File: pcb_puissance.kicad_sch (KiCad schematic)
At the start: 29 parts, among them J1 1735882, J2 1735882, J3 1735882, J4 1735882, J5 1735882, J6 1735882, J7 1735882, J8 1735882, K1 SRD-05VDC-SL-C

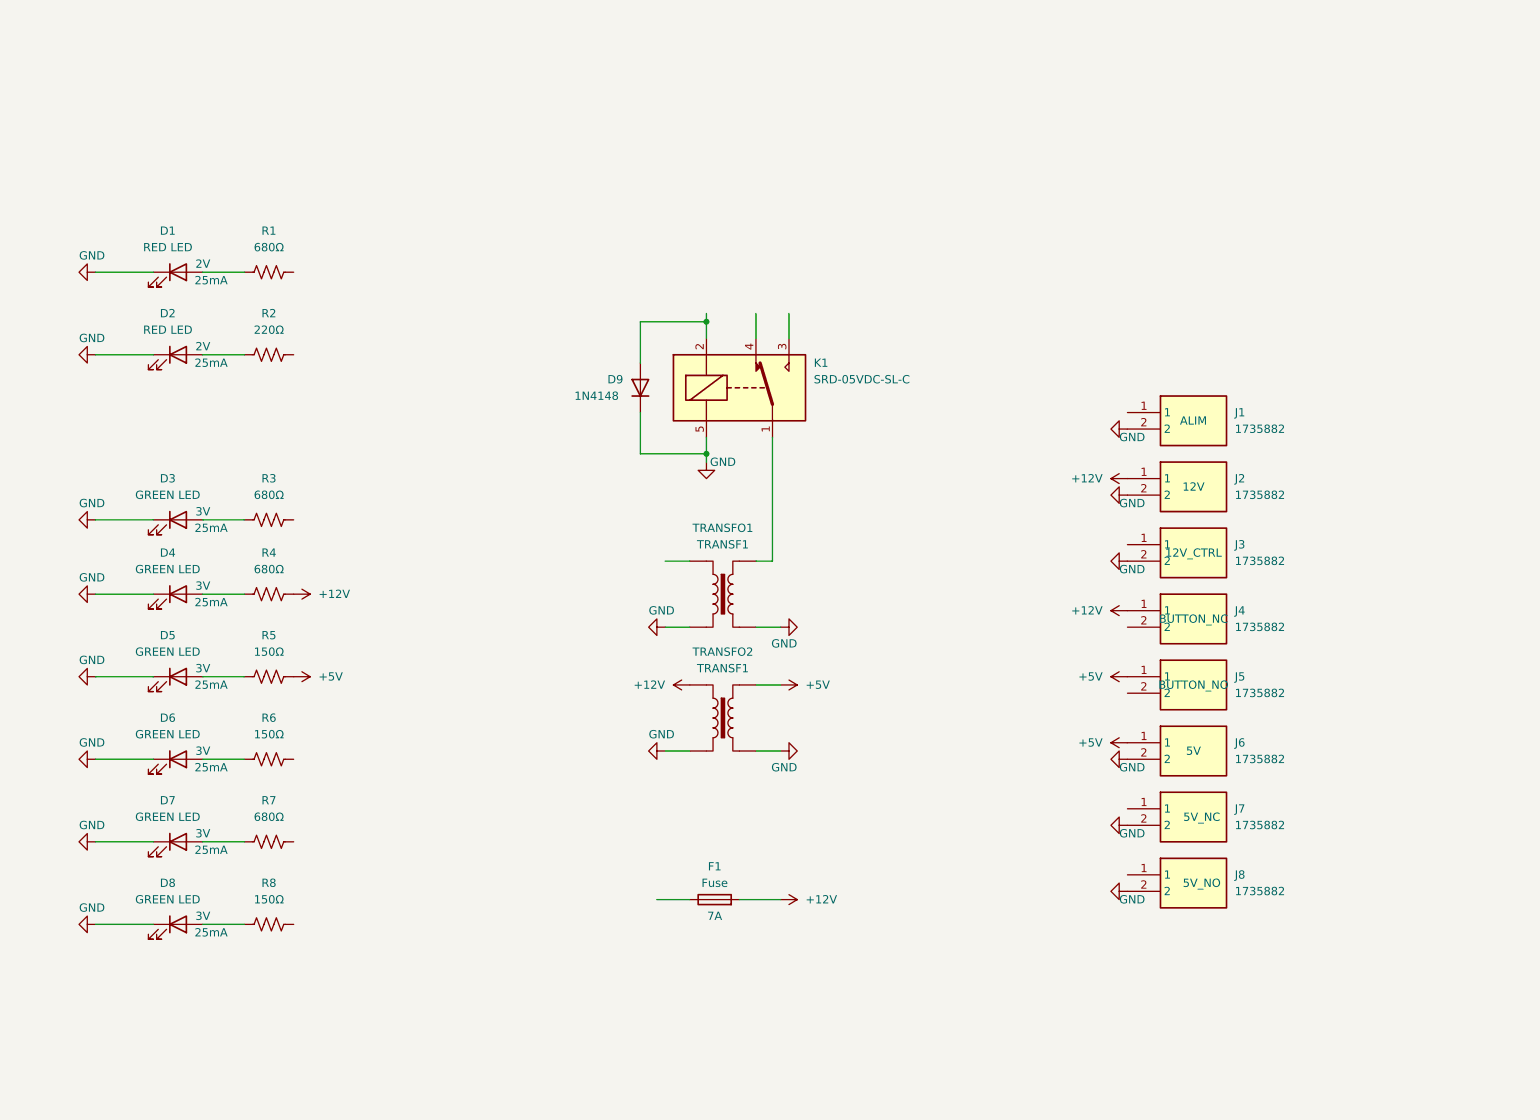
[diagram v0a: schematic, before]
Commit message: changements connecteur CI + placement empreintes et routage PCB
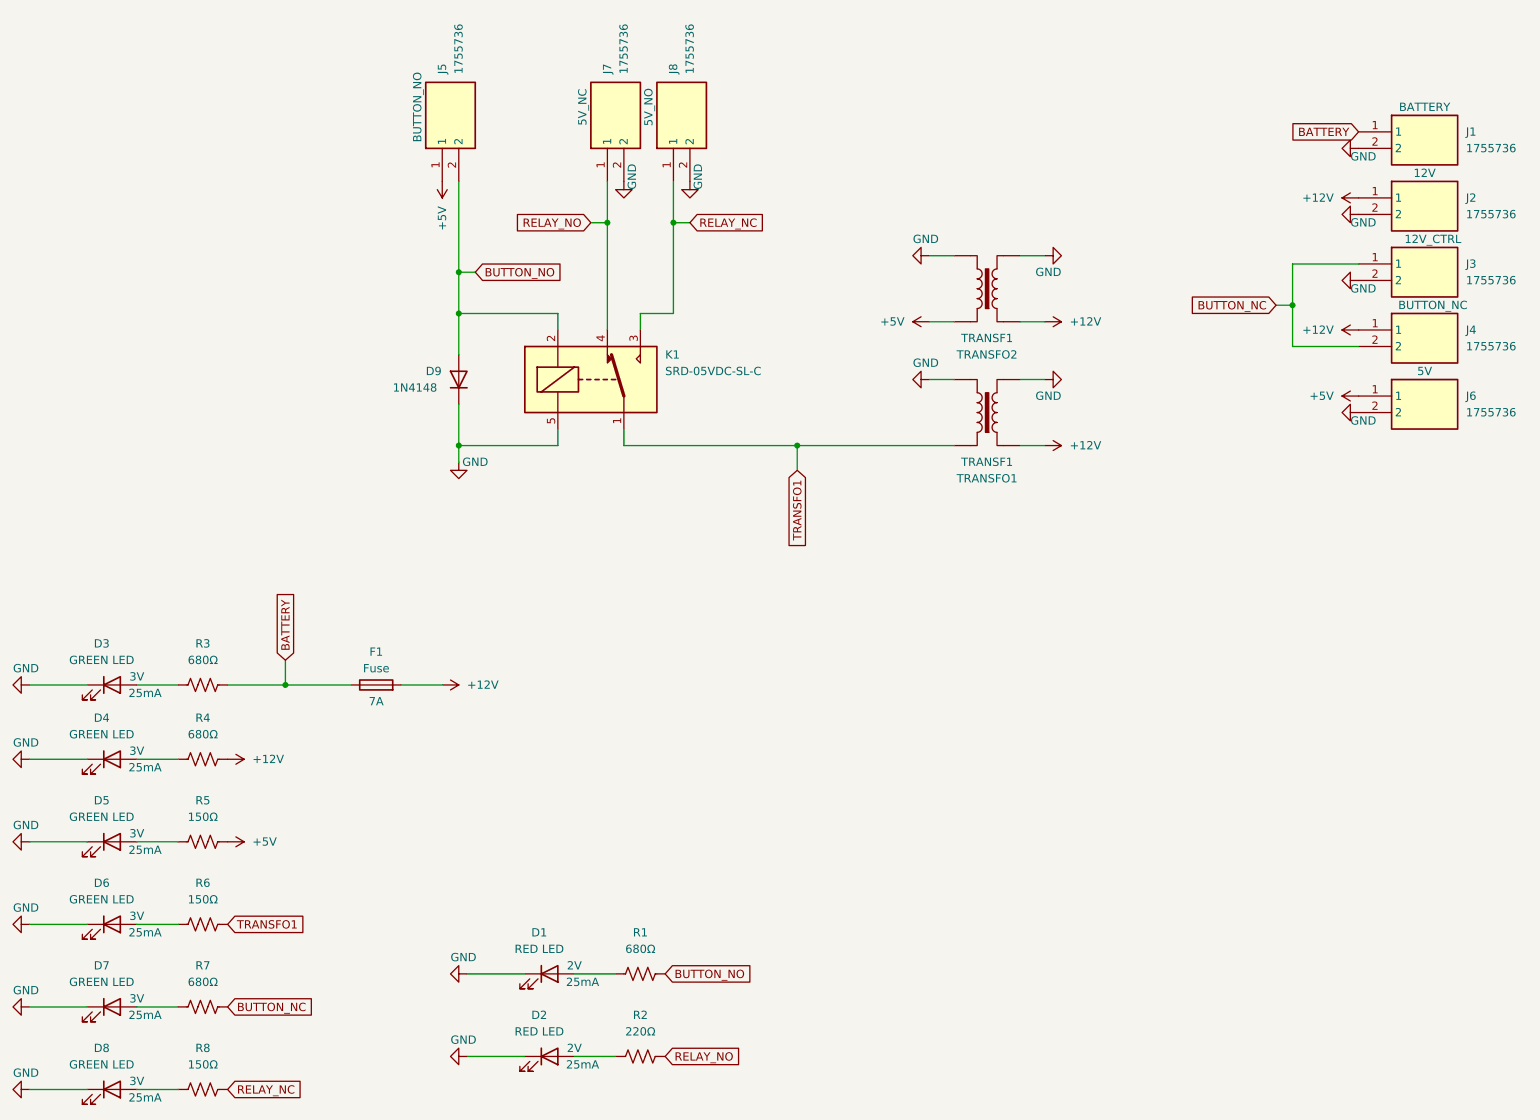
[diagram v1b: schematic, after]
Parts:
- removed J1, J2, J3, J4, J5, J6, J7, J8: 1735882, Library:1735882, symbol New_Library:1735882
- added J1, J2, J3, J4, J5, J6, J7, J8: 1755736, Library:1755736, symbol New_Library:1755736
- D1, D7: Name (none) -> BUTTON
- D2, D8: Name (none) -> RELAY
- D3: Name (none) -> BATTERY
- D4: Name (none) -> 12V
- D5: Name (none) -> 5V
- D6: Name (none) -> TRANSFO1
- F1: footprint (none) -> Library:porte fusible E44
- TRANSFO1, TRANSFO2: footprint (none) -> Library:transfo
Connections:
- net +12V: now also TRANSFO1.1, J2.1, J4.1
- net +5V: now also J5.1, J6.1
- net GND: now also J1.2, J2.2, J3.2, J6.2, J7.2, J8.2
- net BATTERY: now reaches F1.1
- net BATTERY: now also R3.2, J1.1
- net TRANSFO1: now reaches K1.1, TRANSFO1.4
- net TRANSFO1: now also R6.2
- net BUTTON_NO: now reaches D9.2 (A), K1.2
- net BUTTON_NO: now also R1.2, J5.2
- net RELAY_NC: now reaches K1.3
- net RELAY_NC: now also R8.2, J8.1
- net RELAY_NO: now reaches K1.4
- net RELAY_NO: now also R2.2, J7.1
- net BUTTON_NC: now reaches R7.2
- net BUTTON_NC: now also J3.1, J4.2
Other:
- moved on the sheet: D1, D2, D3, D4, D5, D6, D7, D8, D9, F1, K1, R1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

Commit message: Fin routage + contour/plan de masse/entretoises propres.
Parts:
- D6: Name TRANSFO1 -> TRANSFO
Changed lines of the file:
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@@
       (effects (font (size 1.27 1.27)))
     )
-    (property "Name" "TRANSFO1" (at 54.61 156.21 0)
+    (property "Name" "TRANSFO" (at 54.61 156.21 0)
       (effects (font (size 1.27 1.27)) hide)
     )

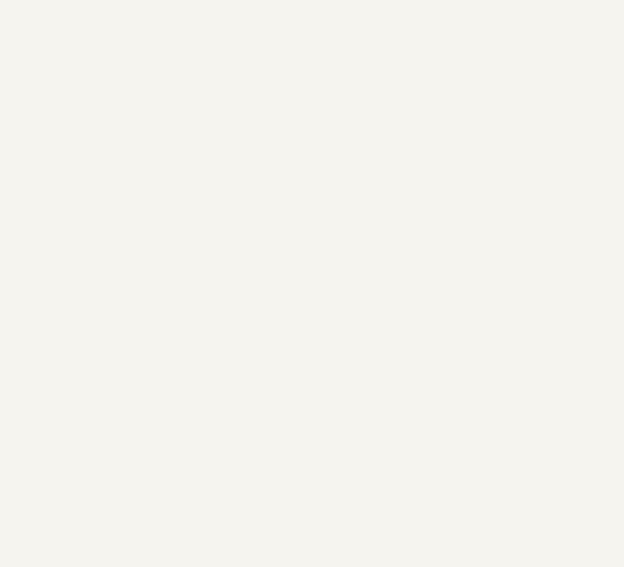
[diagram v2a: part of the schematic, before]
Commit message: Deplacement connecteurs, petites pistes 0.5mm, ajout connecteurs Dupond, plan de masse Front, pastilles pour les fixations
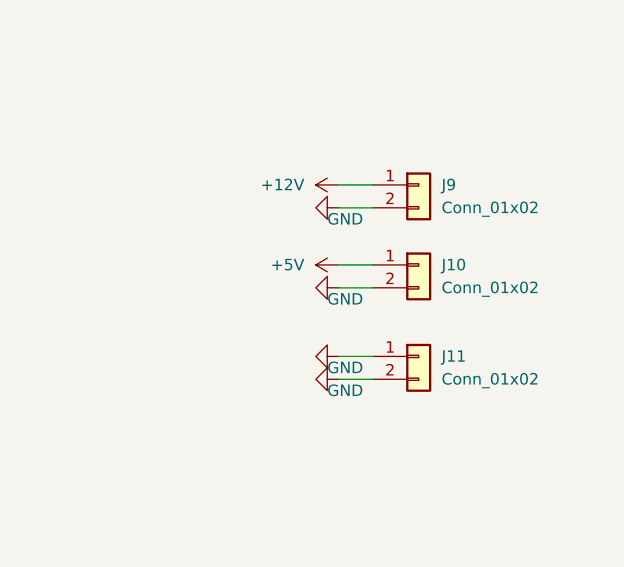
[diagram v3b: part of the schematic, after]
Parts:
- added J10, J11, J9: Conn_01x02, Connector_PinHeader_2.54mm:PinHeader_1x02_P2.54mm_Vertical, symbol Connector_Generic:Conn_01x02
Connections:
- net +12V: now also J9.1 (Pin_1)
- net +5V: now also J10.1 (Pin_1)
- net GND: now also J10.2 (Pin_2), J11.1 (Pin_1), J11.2 (Pin_2), J9.2 (Pin_2)
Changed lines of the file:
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@@
+    (stroke (width 0) (type default))
+  )
+  (wire (pts (xy 242.57 110.49) (xy 246.38 110.49))
     (stroke (width 0) (type default))
   )
@@
     (stroke (width 0) (type default))
   )
+  (wire (pts (xy 242.57 113.03) (xy 246.38 113.03))
+    (stroke (width 0) (type default))
+  )
   (wire (pts (xy 180.34 63.5) (xy 184.15 63.5))
     (stroke (width 0) (type default))
@@
     (stroke (width 0) (type default))
   )
+  (wire (pts (xy 242.57 129.54) (xy 246.38 129.54))
+    (stroke (width 0) (type default))
+  )
+  (wire (pts (xy 242.57 121.92) (xy 246.38 121.92))
+    (stroke (width 0) (type default))
+  )
   (wire (pts (xy 140.97 41.91) (xy 140.97 48.26))
     (stroke (width 0) (type default))
@@
   )
   (wire (pts (xy 233.68 60.96) (xy 236.22 60.96))
+    (stroke (width 0) (type default))
+  )
+  (wire (pts (xy 242.57 132.08) (xy 246.38 132.08))
+    (stroke (width 0) (type default))
+  )
+  (wire (pts (xy 242.57 119.38) (xy 246.38 119.38))
     (stroke (width 0) (type default))
   )
@@
     )
   )
+  (symbol (lib_id "Connector_Generic:Conn_01x02") (at 251.46 110.49 0) (unit 1)
+    (in_bom yes) (on_board yes) (dnp no) (fields_autoplaced)
+    (property "Reference" "J9" (at 254 110.49 0)
+      (effects (font (size 1.27 1.27)) (justify left))
+    )
+    (property "Value" "Conn_01x02" (at 254 113.03 0)
+      (effects (font (size 1.27 1.27)) (justify left))
+    )
+    (property "Footprint" "Connector_PinHeader_2.54mm:PinHeader_1x02_P2.54mm_Vertical" (at 251.46 110.49 0)
+      (effects (font (size 1.27 1.27)) hide)
+    )
+    (property "Datasheet" "~" (at 251.46 110.49 0)
+      (effects (font (size 1.27 1.27)) hide)
+    )
+    (pin "2")
+    (pin "1")
+    (instances
+      (project "pcb_puissance"
+        (path "/e9cf362a-cefc-43a9-90ea-df8ba9531768"
+          (reference "J9") (unit 1)
+        )
+      )
+    )
+  )
+  (symbol (lib_id "Connector_Generic:Conn_01x02") (at 251.46 129.54 0) (unit 1)
+    (in_bom yes) (on_board yes) (dnp no) (fields_autoplaced)
+    (property "Reference" "J11" (at 254 129.54 0)
+      (effects (font (size 1.27 1.27)) (justify left))
+    )
+    (property "Value" "Conn_01x02" (at 254 132.08 0)
+      (effects (font (size 1.27 1.27)) (justify left))
+    )
+    (property "Footprint" "Connector_PinHeader_2.54mm:PinHeader_1x02_P2.54mm_Vertical" (at 251.46 129.54 0)
+      (effects (font (size 1.27 1.27)) hide)
+    )
+    (property "Datasheet" "~" (at 251.46 129.54 0)
+      (effects (font (size 1.27 1.27)) hide)
+    )
+    (pin "2")
+    (pin "1")
+    (instances
+      (project "pcb_puissance"
+        (path "/e9cf362a-cefc-43a9-90ea-df8ba9531768"
+          (reference "J11") (unit 1)
+        )
+      )
+    )
+  )
   (symbol (lib_id "New_Library:1755736") (at 246.38 44.45 0) (unit 1)
     (in_bom yes) (on_board yes) (dnp no)
@@
     )
   )
+  (symbol (lib_id "power:+12V") (at 242.57 110.49 90) (unit 1)
+    (in_bom yes) (on_board yes) (dnp no) (fields_autoplaced)
+    (property "Reference" "#PWR035" (at 246.38 110.49 0)
+      (effects (font (size 1.27 1.27)) hide)
+    )
+    (property "Value" "+12V" (at 238.76 110.49 90)
+      (effects (font (size 1.27 1.27)) (justify left))
+    )
+    (property "Footprint" "" (at 242.57 110.49 0)
+      (effects (font (size 1.27 1.27)) hide)
+    )
+    (property "Datasheet" "" (at 242.57 110.49 0)
+      (effects (font (size 1.27 1.27)) hide)
+    )
+    (pin "1")
+    (instances
+      (project "pcb_puissance"
+        (path "/e9cf362a-cefc-43a9-90ea-df8ba9531768"
+          (reference "#PWR035") (unit 1)
+        )
+      )
+    )
+  )
   (symbol (lib_id "New_Library:1755736") (at 105.41 41.91 90) (unit 1)
     (in_bom yes) (on_board yes) (dnp no)
@@
     )
   )
+  (symbol (lib_id "power:+5V") (at 242.57 119.38 90) (unit 1)
+    (in_bom yes) (on_board yes) (dnp no) (fields_autoplaced)
+    (property "Reference" "#PWR033" (at 246.38 119.38 0)
+      (effects (font (size 1.27 1.27)) hide)
+    )
+    (property "Value" "+5V" (at 238.76 119.38 90)
+      (effects (font (size 1.27 1.27)) (justify left))
+    )
+    (property "Footprint" "" (at 242.57 119.38 0)
+      (effects (font (size 1.27 1.27)) hide)
+    )
+    (property "Datasheet" "" (at 242.57 119.38 0)
+      (effects (font (size 1.27 1.27)) hide)
+    )
+    (pin "1")
+    (instances
+      (project "pcb_puissance"
+        (path "/e9cf362a-cefc-43a9-90ea-df8ba9531768"
+          (reference "#PWR033") (unit 1)
+        )
+      )
+    )
+  )
   (symbol (lib_id "Device:R_US") (at 68.58 168.91 90) (unit 1)
     (in_bom yes) (on_board yes) (dnp no) (fields_autoplaced)
@@
     )
   )
+  (symbol (lib_id "power:GND") (at 242.57 132.08 270) (unit 1)
+    (in_bom yes) (on_board yes) (dnp no)
+    (property "Reference" "#PWR030" (at 236.22 132.08 0)
+      (effects (font (size 1.27 1.27)) hide)
+    )
+    (property "Value" "GND" (at 241.3 133.35 90)
+      (effects (font (size 1.27 1.27)) (justify left))
+    )
+    (property "Footprint" "" (at 242.57 132.08 0)
+      (effects (font (size 1.27 1.27)) hide)
+    )
+    (property "Datasheet" "" (at 242.57 132.08 0)
+      (effects (font (size 1.27 1.27)) hide)
+    )
+    (pin "1")
+    (instances
+      (project "pcb_puissance"
+        (path "/e9cf362a-cefc-43a9-90ea-df8ba9531768"
+          (reference "#PWR030") (unit 1)
+        )
+      )
+    )
+  )
   (symbol (lib_id "Transformer:TRANSF1") (at 189.23 77.47 180) (unit 1)
     (in_bom yes) (on_board yes) (dnp no) (fields_autoplaced)
@@
     )
   )
+  (symbol (lib_id "Connector_Generic:Conn_01x02") (at 251.46 119.38 0) (unit 1)
+    (in_bom yes) (on_board yes) (dnp no) (fields_autoplaced)
+    (property "Reference" "J10" (at 254 119.38 0)
+      (effects (font (size 1.27 1.27)) (justify left))
+    )
+    (property "Value" "Conn_01x02" (at 254 121.92 0)
+      (effects (font (size 1.27 1.27)) (justify left))
+    )
+    (property "Footprint" "Connector_PinHeader_2.54mm:PinHeader_1x02_P2.54mm_Vertical" (at 251.46 119.38 0)
+      (effects (font (size 1.27 1.27)) hide)
+    )
+    (property "Datasheet" "~" (at 251.46 119.38 0)
+      (effects (font (size 1.27 1.27)) hide)
+    )
+    (pin "2")
+    (pin "1")
+    (instances
+      (project "pcb_puissance"
+        (path "/e9cf362a-cefc-43a9-90ea-df8ba9531768"
+          (reference "J10") (unit 1)
+        )
+      )
+    )
+  )
   (symbol (lib_id "Device:LED") (at 54.61 130.81 0) (unit 1)
     (in_bom yes) (on_board yes) (dnp no)
@@
     )
   )
+  (symbol (lib_id "power:GND") (at 242.57 121.92 270) (unit 1)
+    (in_bom yes) (on_board yes) (dnp no)
+    (property "Reference" "#PWR031" (at 236.22 121.92 0)
+      (effects (font (size 1.27 1.27)) hide)
+    )
+    (property "Value" "GND" (at 241.3 123.19 90)
+      (effects (font (size 1.27 1.27)) (justify left))
+    )
+    (property "Footprint" "" (at 242.57 121.92 0)
+      (effects (font (size 1.27 1.27)) hide)
+    )
+    (property "Datasheet" "" (at 242.57 121.92 0)
+      (effects (font (size 1.27 1.27)) hide)
+    )
+    (pin "1")
+    (instances
+      (project "pcb_puissance"
+        (path "/e9cf362a-cefc-43a9-90ea-df8ba9531768"
+          (reference "#PWR031") (unit 1)
+        )
+      )
+    )
+  )
   (symbol (lib_id "New_Library:1755736") (at 246.38 74.93 0) (unit 1)
     (in_bom yes) (on_board yes) (dnp no)
@@
         )
       )
+    )
+  )
+  (symbol (lib_id "power:GND") (at 242.57 129.54 270) (unit 1)
+    (in_bom yes) (on_board yes) (dnp no)
+    (property "Reference" "#PWR034" (at 236.22 129.54 0)
+      (effects (font (size 1.27 1.27)) hide)
+    )
+    (property "Value" "GND" (at 241.3 130.81 90)
+      (effects (font (size 1.27 1.27)) (justify left))
+    )
+    (property "Footprint" "" (at 242.57 129.54 0)
+      (effects (font (size 1.27 1.27)) hide)
+    )
+    (property "Datasheet" "" (at 242.57 129.54 0)
+      (effects (font (size 1.27 1.27)) hide)
+    )
+    (pin "1")
+    (instances
+      (project "pcb_puissance"
+        (path "/e9cf362a-cefc-43a9-90ea-df8ba9531768"
+          (reference "#PWR034") (unit 1)
+        )
+      )
+    )
+  )
+  (symbol (lib_id "power:GND") (at 242.57 113.03 270) (unit 1)
+    (in_bom yes) (on_board yes) (dnp no)
+    (property "Reference" "#PWR032" (at 236.22 113.03 0)
+      (effects (font (size 1.27 1.27)) hide)
+    )
+    (property "Value" "GND" (at 241.3 114.3 90)
+      (effects (font (size 1.27 1.27)) (justify left))
+    )
+    (property "Footprint" "" (at 242.57 113.03 0)
+      (effects (font (size 1.27 1.27)) hide)
+    )
+    (property "Datasheet" "" (at 242.57 113.03 0)
+      (effects (font (size 1.27 1.27)) hide)
+    )
+    (pin "1")
+    (instances
+      (project "pcb_puissance"
+        (path "/e9cf362a-cefc-43a9-90ea-df8ba9531768"
+          (reference "#PWR032") (unit 1)
+        )
+      )

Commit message: Fixations
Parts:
- removed TRANSFO1, TRANSFO2: TRANSF1, Library:transfo, symbol Transformer:TRANSF1
- added Fix1, Fix2, Fix3, Fix4, Fix5, Fix6: ~, Library:FIX3.2P7.5, symbol New_Library:FIX3.2P7.5
- added TRANSFO1, TRANSFO2: TRANSF1, Library:transfo, symbol New_Library:TRANSF1
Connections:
- net +12V: now also TRANSFO1.1 (Primaire_+), TRANSFO2.1 (Primaire_+)
- net +5V: now also TRANSFO2.4 (Secondaire_+)
- net GND: now also Fix1.1, Fix2.1, Fix3.1, Fix4.1, Fix5.1, Fix6.1, TRANSFO1.2 (Primaire_GND), TRANSFO1.3 (Secondaire_GND), TRANSFO1.5 (Fix), TRANSFO2.2 (Primaire_GND), TRANSFO2.3 (Secondaire_GND), TRANSFO2.5 (Fix)
- net TRANSFO1: now also TRANSFO1.4 (Secondaire_+)
